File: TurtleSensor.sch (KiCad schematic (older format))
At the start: 13 parts, among them IC1 ATMEGA328P-A, J1 ISPConnector, J2 FTDIConnector, U1 SI7021, U2 W25Q32FVSSIG

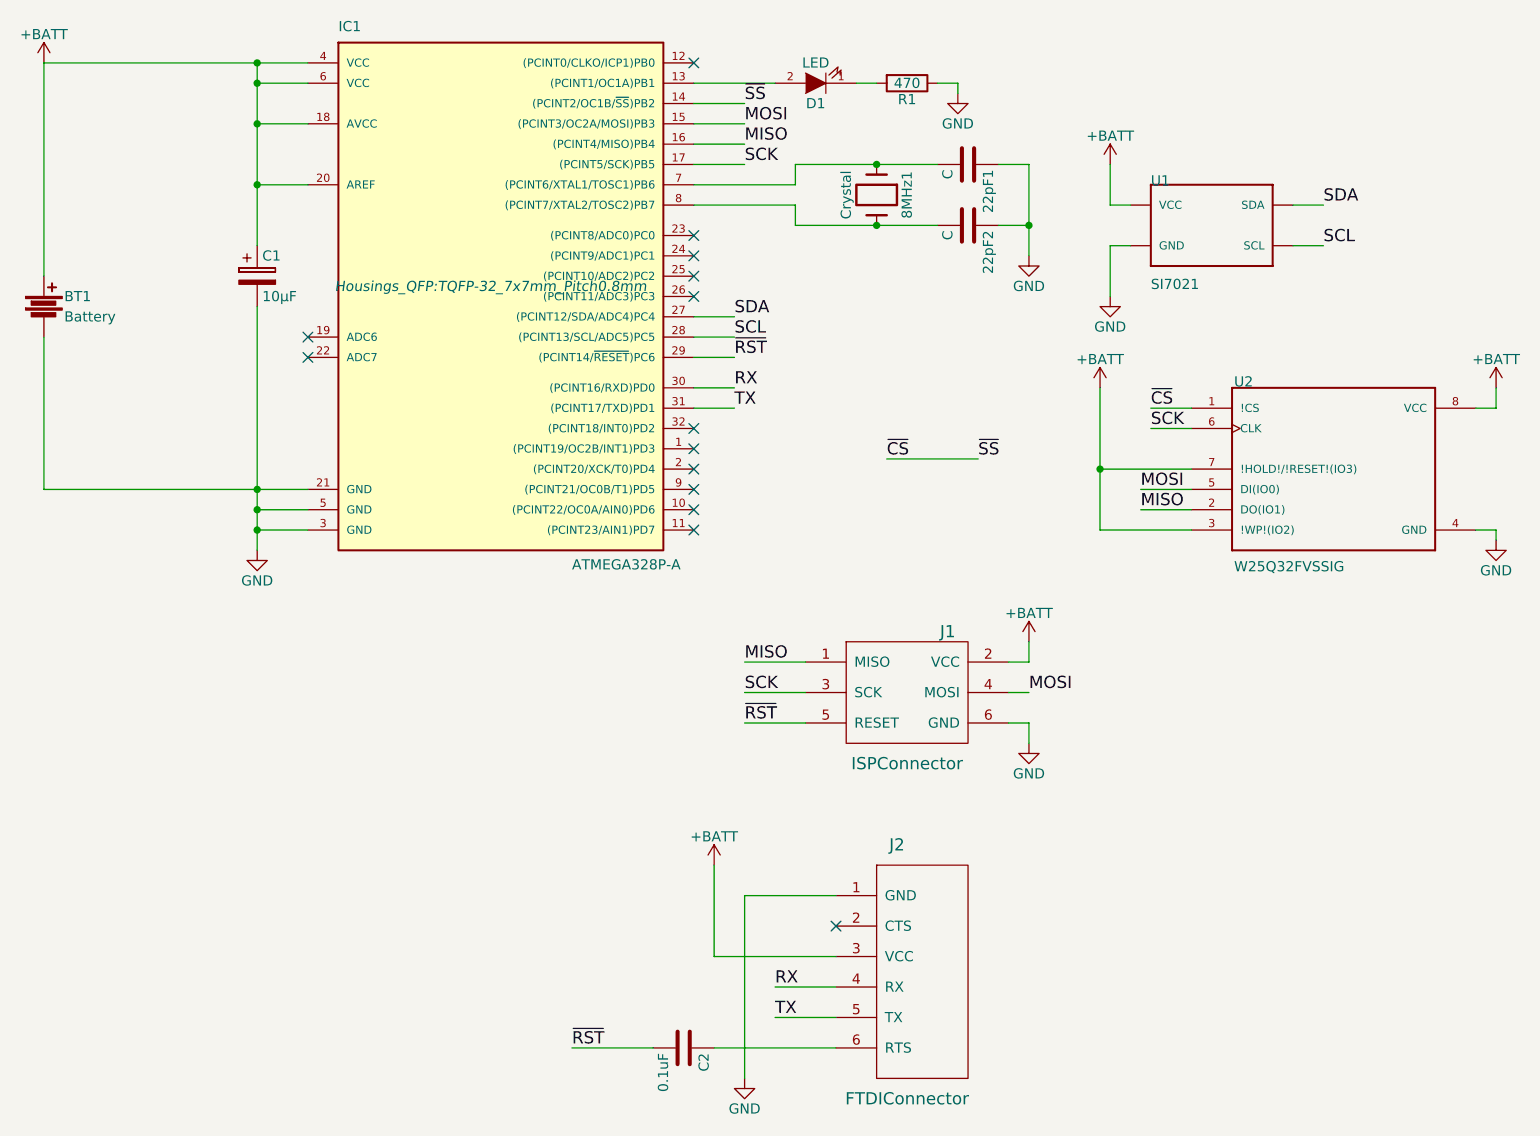
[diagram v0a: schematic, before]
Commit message: pads underneath flash short
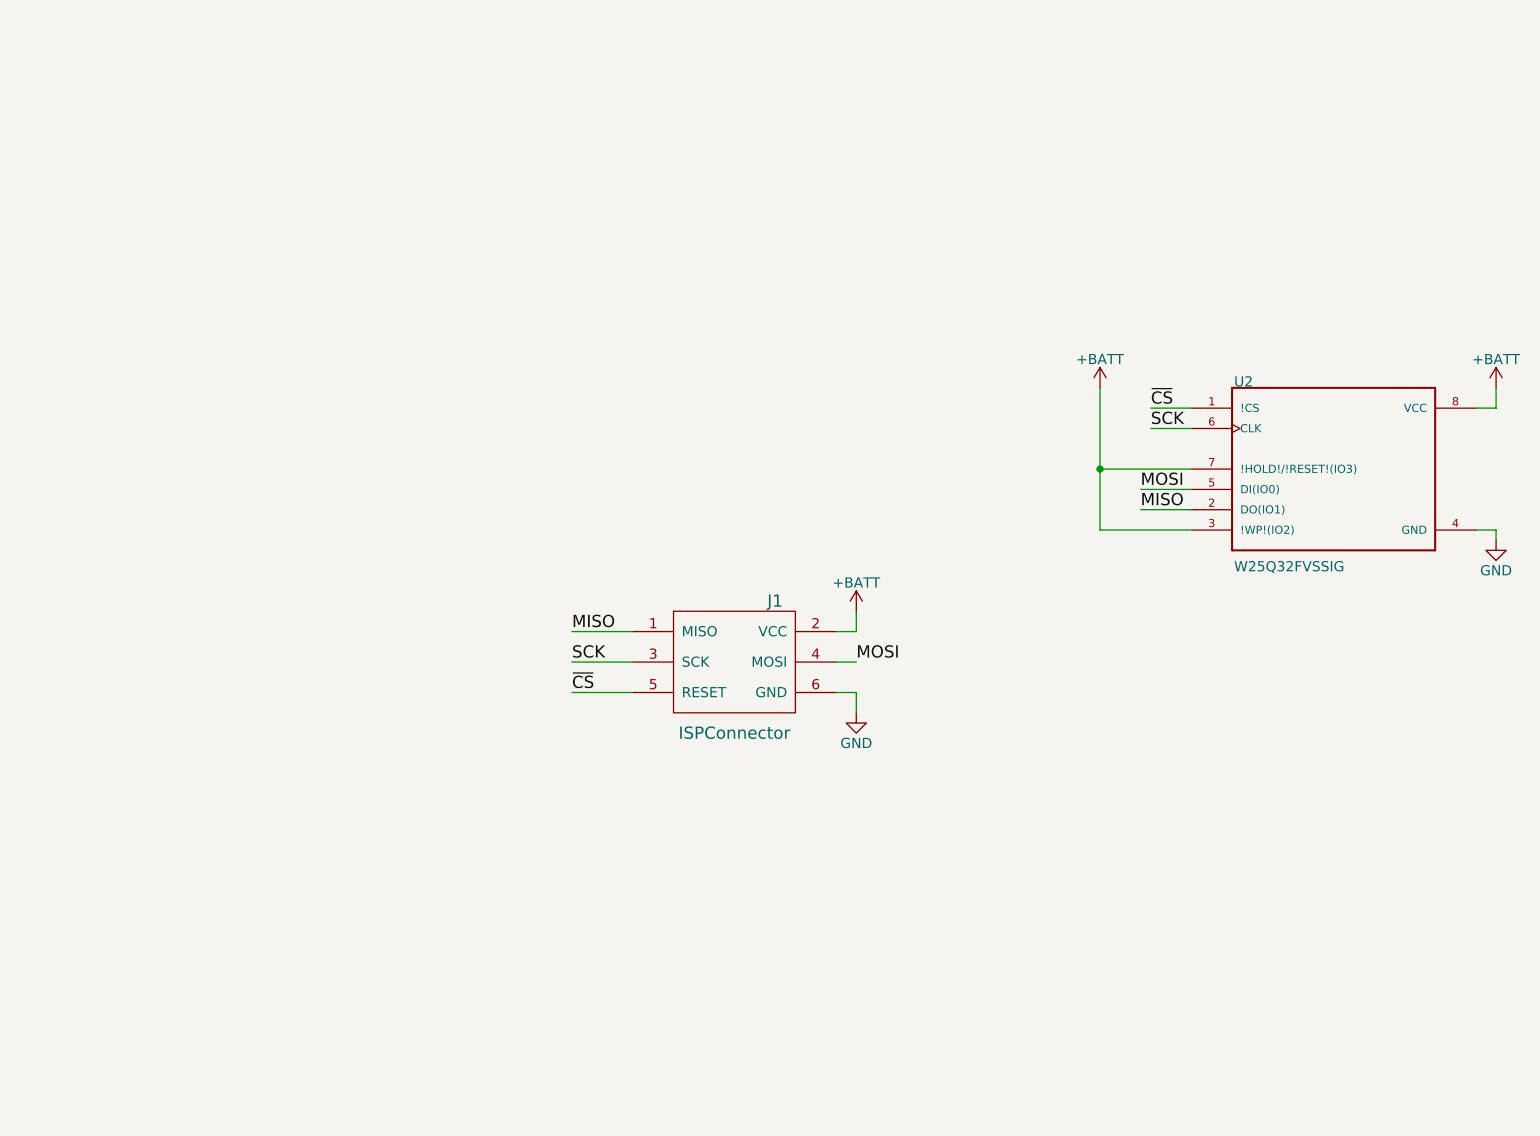
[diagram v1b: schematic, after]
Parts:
- removed 22pF1, 22pF2: C, Capacitors_SMD:C_0805_HandSoldering, symbol C
- removed 8MHz1: Crystal, Crystals:Crystal_HC49-SD_SMD, symbol Crystal
- removed BT1: Battery, Socket_Strips:Socket_Strip_Straight_1x02, symbol Battery
- removed C1: 10µF, Capacitors_SMD:C_0805_HandSoldering, symbol CP
- removed C2: 0.1uF, Capacitors_SMD:C_0805_HandSoldering, symbol C
- removed D1: LED, LEDs:LED_0805, symbol LED
- removed IC1: ATMEGA328P-A, Housings_QFP:TQFP-32_7x7mm_Pitch0.8mm, symbol ATMEGA328P-A
- removed J2: FTDIConnector, Socket_Strips:Socket_Strip_Angled_1x06, symbol FTDIConnector
- removed R1: 470, Resistors_SMD:R_0805_HandSoldering, symbol R
- removed U1: SI7021, SI7021:DFN-6%2f3MM, symbol SI7021
- J1: footprint Socket_Strips:Socket_Strip_Straight_2x03 -> Socket_Strips:Socket_Strip_Straight_1x06
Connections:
- net ~RST is gone; now on net ~CS: J1.5 (RESET)
- no-connect marks 14 -> 0
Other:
- moved on the sheet: J1
